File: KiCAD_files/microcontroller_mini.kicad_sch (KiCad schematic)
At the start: 36 parts, among them J1 Conn_02x20_Top_Bottom, J2 Molex_47346-0001, J8 FTSH-107-01-F-DV-K, SW1 SW_Push, U1 STM32G474RE, U2 AT25xxx, U3 WE-TVS-82400102, U4 AP1117-33, Y1 ECS-240-10-33-AGM-TR - 24MHz

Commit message: [Feeder] WIP on the V2 redesign
Former-commit-id: 5bce92fb9a428cd005e74b891f189b6460f88472
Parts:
- F1, F2: value 500mA -> 350mA
- FB1: value 100Ohm @ 100MHz -> 1000Ohm @ 100MHz
- SW1: value SW_Push -> KMR241NGLFS
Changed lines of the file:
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@@
     (in_bom yes) (on_board yes)
     (property "Reference" "FB1" (id 0) (at 124.46 31.115 90))
-    (property "Value" "100Ohm @ 100MHz" (id 1) (at 132.08 33.655 90))
+    (property "Value" "1000Ohm @ 100MHz" (id 1) (at 132.08 33.655 90))
     (property "Footprint" "Resistor_SMD:R_0402_1005Metric" (id 2) (at 147.955 35.052 90)
       (effects (font (size 1.27 1.27)) hide)
@@
       (effects (font (size 1.27 1.27)) (justify right) hide)
     )
-    (property "Value" "SW_Push" (id 1) (at 65.9892 86.233 90)
-      (effects (font (size 1.27 1.27)) (justify right))
+    (property "Value" "KMR241NGLFS" (id 1) (at 65.9892 86.233 90)
+      (effects (font (size 1.27 1.27)) (justify right) hide)
     )
     (property "Footprint" "Button_Switch_SMD:SW_Push_1P1T_NO_CK_KMR2" (id 2) (at 59.69 85.09 0)
@@
     (in_bom yes) (on_board yes)
     (property "Reference" "F2" (id 0) (at 247.65 112.395 0))
-    (property "Value" "500mA" (id 1) (at 248.285 117.475 0))
+    (property "Value" "350mA" (id 1) (at 248.285 117.475 0))
     (property "Footprint" "Fuse:Fuse_0805_2012Metric" (id 2) (at 247.65 115.57 0)
       (effects (font (size 1.27 1.27)) hide)
@@
     (in_bom yes) (on_board yes)
     (property "Reference" "F1" (id 0) (at 230.505 69.215 0))
-    (property "Value" "500mA" (id 1) (at 230.505 73.025 0))
+    (property "Value" "350mA" (id 1) (at 230.505 73.025 0))
     (property "Footprint" "Fuse:Fuse_0805_2012Metric" (id 2) (at 230.505 71.12 0)
       (effects (font (size 1.27 1.27)) hide)
@@
     )
     (path "/d75b5b01-b636-4a7a-b0c8-6340d666a7aa"
-      (reference "F1") (unit 1) (value "500mA") (footprint "Fuse:Fuse_0805_2012Metric")
+      (reference "F1") (unit 1) (value "350mA") (footprint "Fuse:Fuse_0805_2012Metric")
     )
     (path "/c3a7ce53-3092-487f-964a-35889c2cca98"
-      (reference "F2") (unit 1) (value "500mA") (footprint "Fuse:Fuse_0805_2012Metric")
+      (reference "F2") (unit 1) (value "350mA") (footprint "Fuse:Fuse_0805_2012Metric")
     )
     (path "/00000000-0000-0000-0000-000060f3113e"
-      (reference "FB1") (unit 1) (value "100Ohm @ 100MHz") (footprint "Resistor_SMD:R_0402_1005Metric")
+      (reference "FB1") (unit 1) (value "1000Ohm @ 100MHz") (footprint "Resistor_SMD:R_0402_1005Metric")
     )
     (path "/6d462d91-4a37-4b66-9681-55aedddcb95b"
@@
     )
     (path "/00000000-0000-0000-0000-0000614b9634"
-      (reference "SW1") (unit 1) (value "SW_Push") (footprint "Button_Switch_SMD:SW_Push_1P1T_NO_CK_KMR2")
+      (reference "SW1") (unit 1) (value "KMR241NGLFS") (footprint "Button_Switch_SMD:SW_Push_1P1T_NO_CK_KMR2")
     )
     (path "/00000000-0000-0000-0000-00006163b4d7"

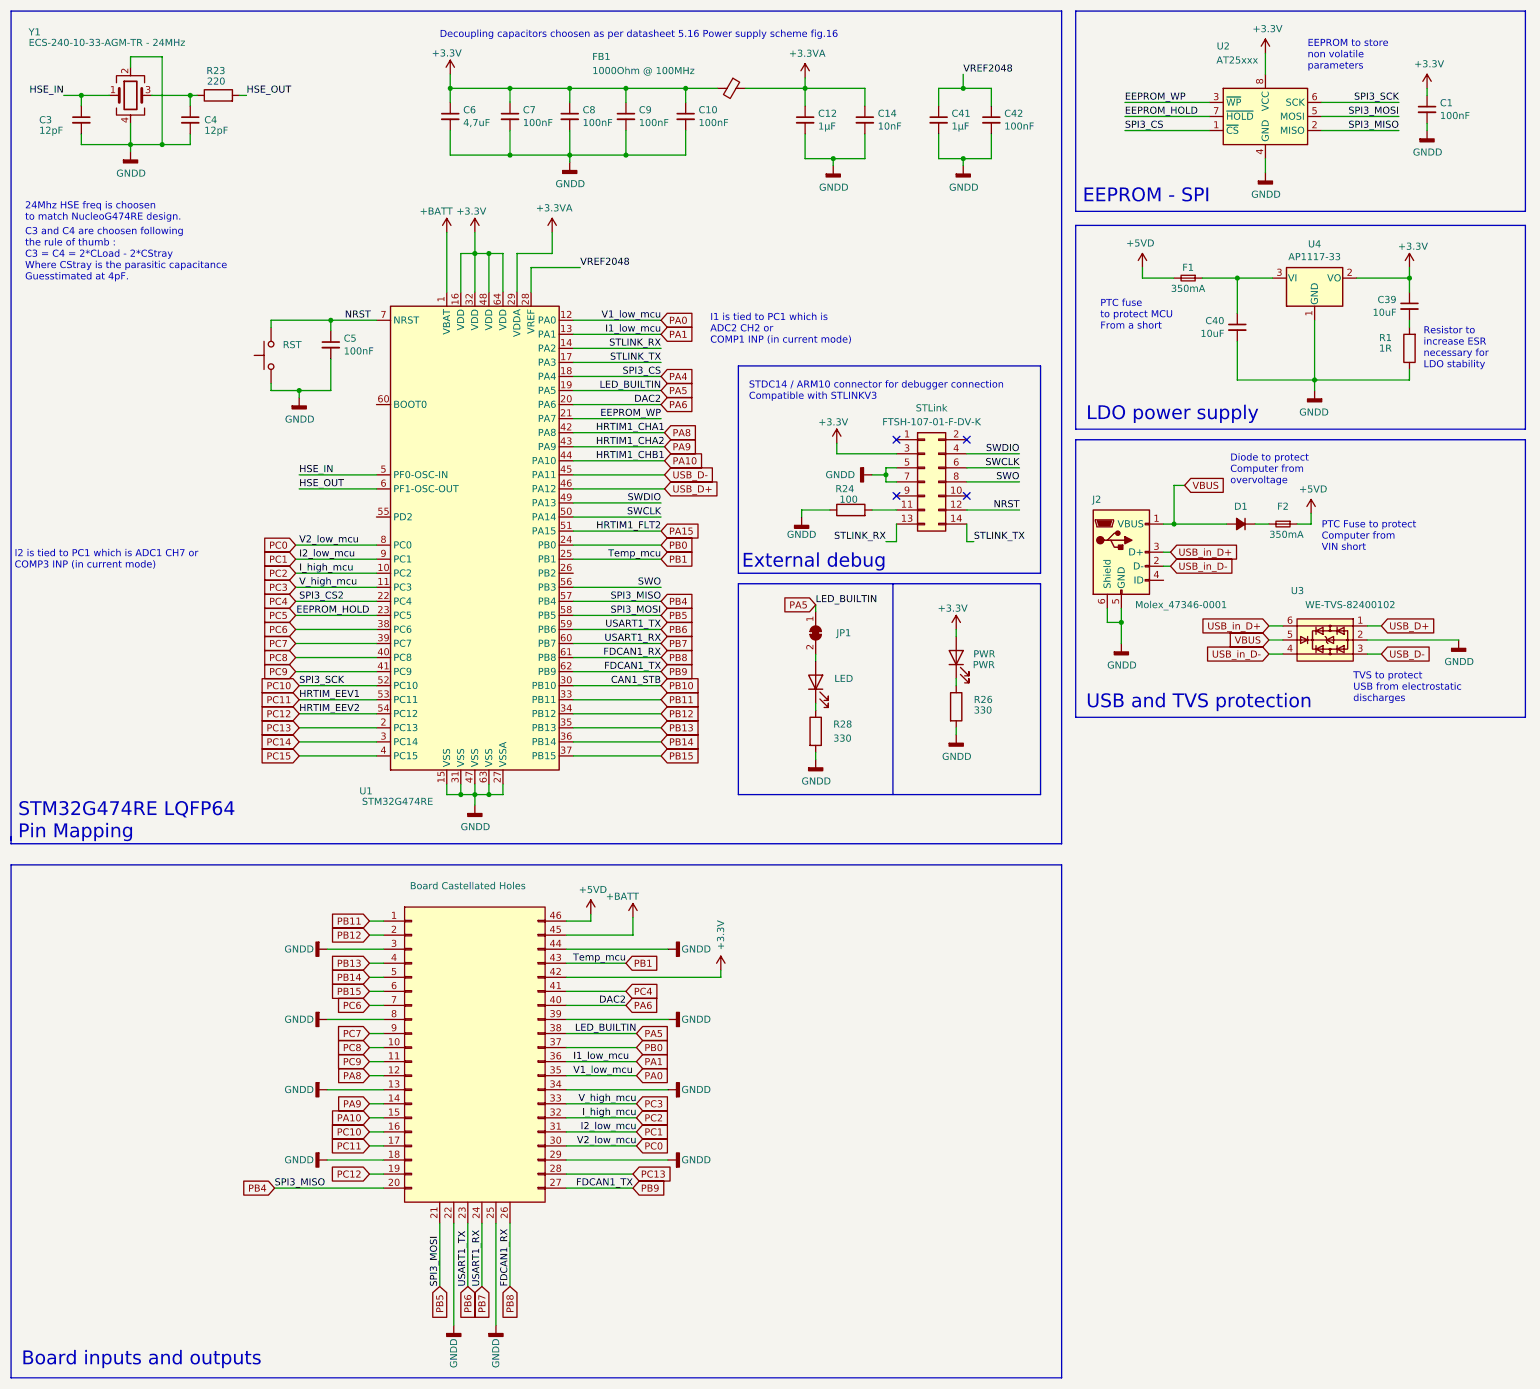
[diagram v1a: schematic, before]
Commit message: WIP : Started correcting MCU board mistakes
Former-commit-id: 0e34b6d72e10d1eac13c8cf31fc8e8f14d7f468b
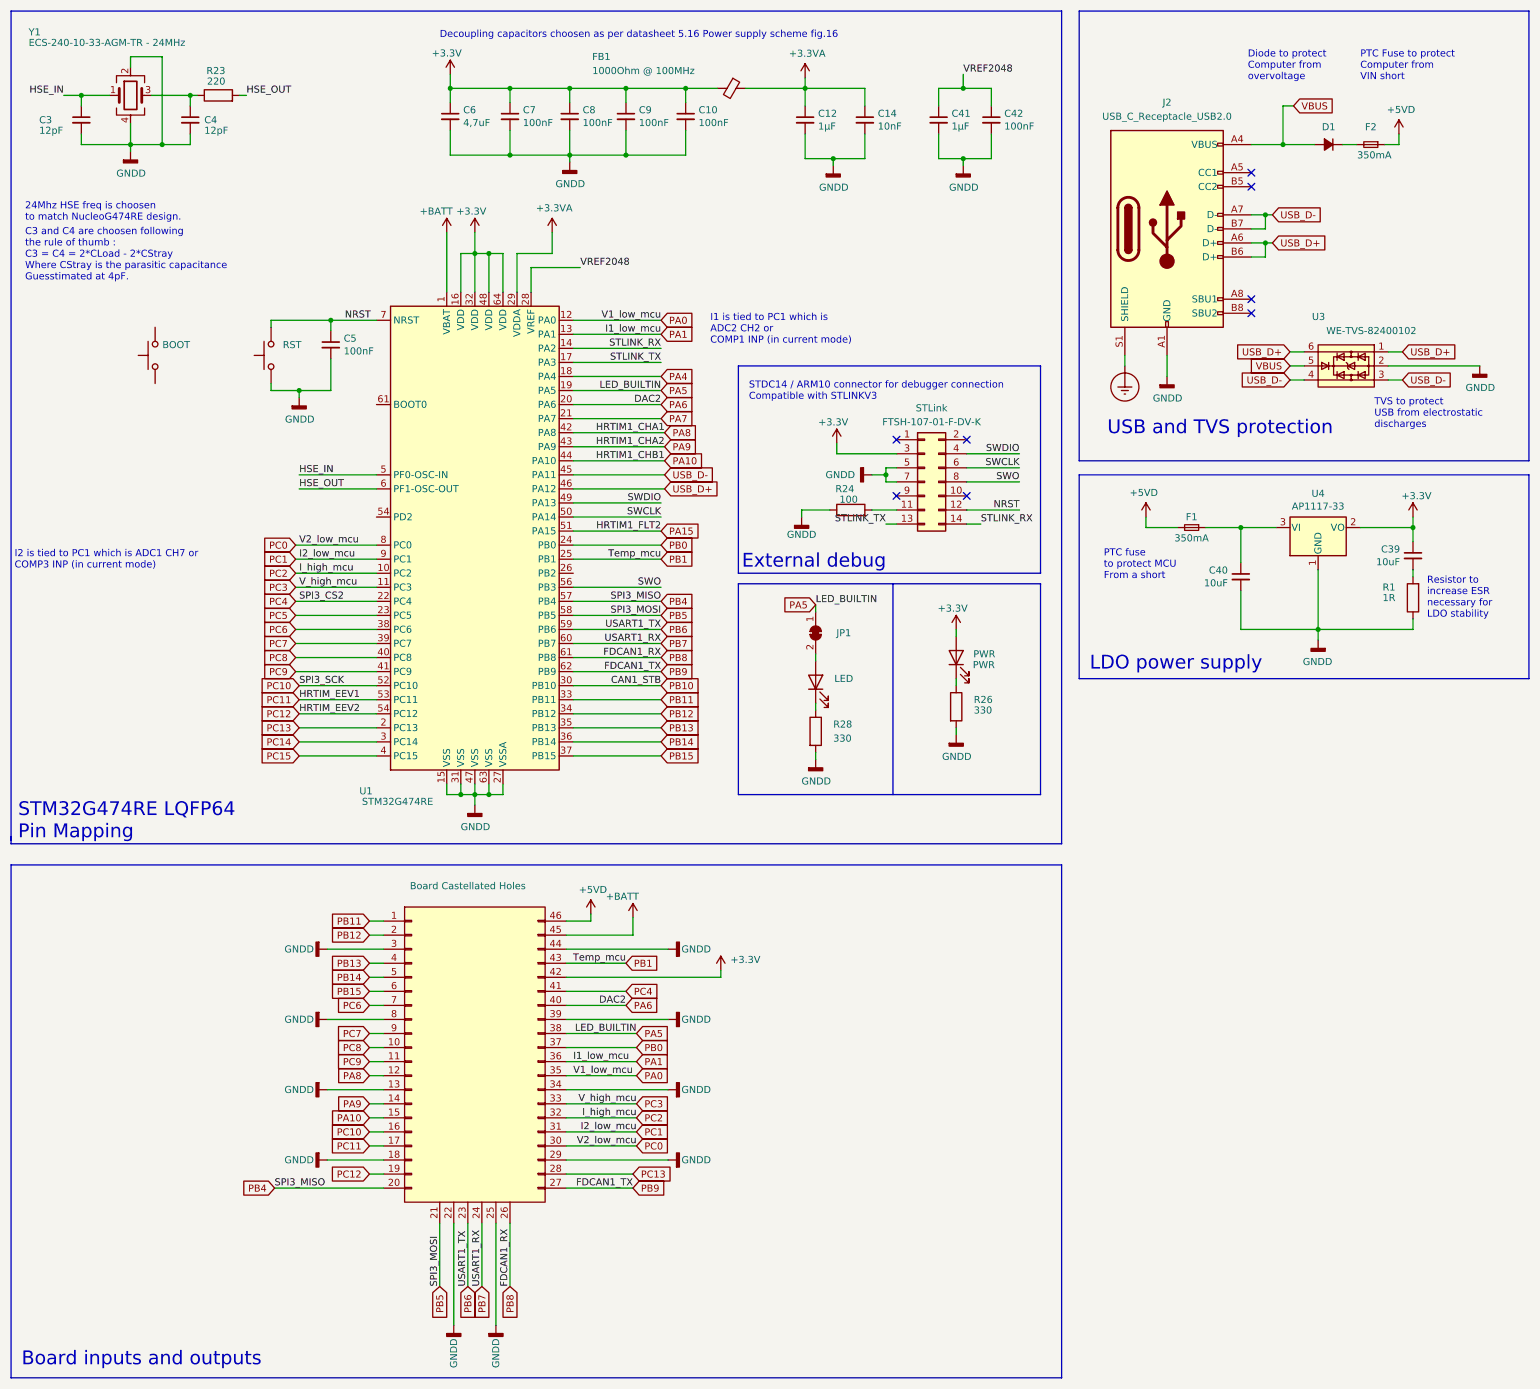
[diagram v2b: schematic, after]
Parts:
- removed C1: 100nF, Capacitor_SMD:C_0402_1005Metric, symbol Device:C_Small
- removed J2: Molex_47346-0001, Connector_USB:USB_Micro-B_Molex_47346-0001, symbol Connector:USB_B_Micro
- removed U2: AT25xxx, Footprints:SOIC-8_3.9x4.9mm_P1.27mm, symbol Memory_EEPROM:AT25xxx
- added J2: USB_C_Receptacle_USB2.0, Connector_USB:USB_C_Receptacle_HRO_TYPE-C-31-M-12, symbol Connector:USB_C_Receptacle_USB2.0
- added SW2: KMR241NGLFS, Button_Switch_SMD:SW_Push_1P1T_NO_CK_KMR2, symbol Switch:SW_Push
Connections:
- net USB_in_D+ is gone; now on net USB_D+: U3.6
- net USB_in_D- is gone; now on net USB_D-: U3.4
- net GNDD: now also J2.A1 (GND), J2.A12 (GND), J2.B1 (GND), J2.B12 (GND)
- net STLINK_RX: now also J8.14 (Pin_14); no longer J8.13 (Pin_13)
- net STLINK_TX: now also J8.13 (Pin_13); no longer J8.14 (Pin_14)
- net USB_D+: now also J2.A6 (D+), J2.B6 (D+)
- net USB_D-: now also J2.A7 (D-), J2.B7 (D-)
- net VBUS: now also J2.A4 (VBUS), J2.A9 (VBUS), J2.B4 (VBUS), J2.B9 (VBUS)
- net EEPROM_WP renamed PA7
- new net Earth_Protective: J2.S1 (SHIELD)
- no-connect marks 4 -> 8
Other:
- note removed: "EEPROM - SPI"
- note removed: "EEPROM to store non volatile parameters"
- moved on the sheet: C39, C40, F1, R1, U3, U4

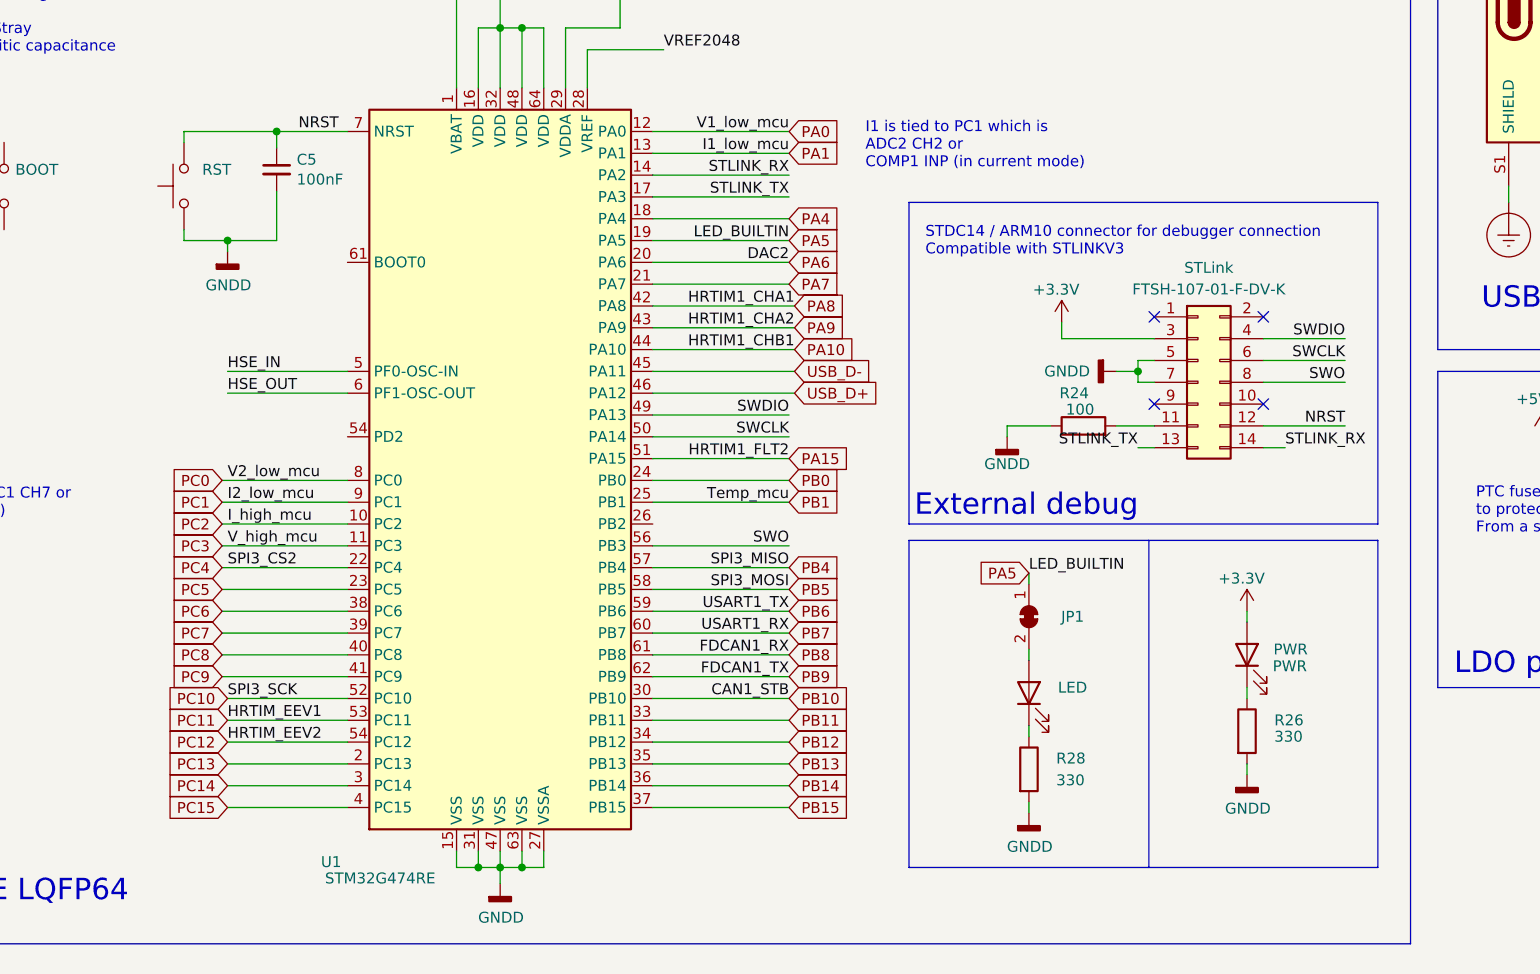
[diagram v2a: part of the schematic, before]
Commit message: WIP: added features for the RJ45 communication link. Added fast RS485 Added HRTIM Sync Added current share analog bus Added external VREF Added dedicated supply power supply pins for the data manager
Former-commit-id: 7d7dbd6688aaf47caa2ea5f91bf9cef552f6a24c
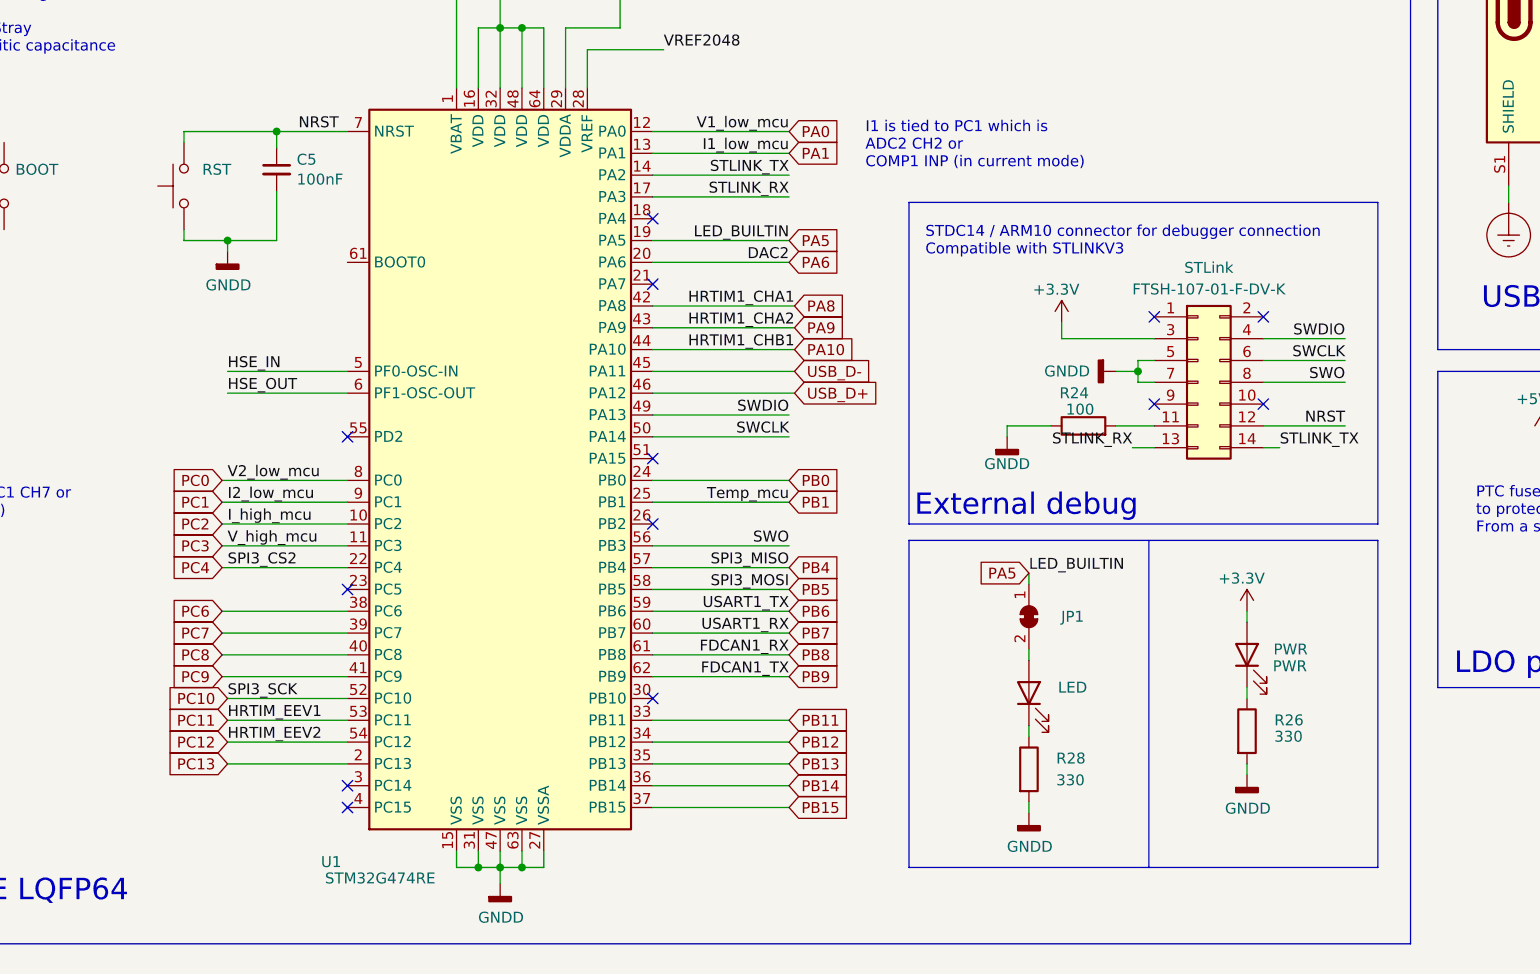
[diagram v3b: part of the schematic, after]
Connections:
- net STLINK_RX: now also J8.13 (Pin_13), U1.17 (PA3); no longer J8.14 (Pin_14), U1.14 (PA2)
- net STLINK_TX: now also J8.14 (Pin_14), U1.14 (PA2); no longer J8.13 (Pin_13), U1.17 (PA3)
- net PA15: no longer names the net of U1.51 (PA15)
- net PA4: no longer names the net of U1.18 (PA4)
- net PA7: no longer names the net of U1.21 (PA7)
- net PB10: no longer names the net of U1.30 (PB10)
- net PC14: no longer names the net of U1.3 (PC14)
- net PC15: no longer names the net of U1.4 (PC15)
- net PC5: no longer names the net of U1.23 (PC5)
- no-connect marks 8 -> 17
